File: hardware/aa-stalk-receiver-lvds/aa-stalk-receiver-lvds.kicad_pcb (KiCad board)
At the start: 2 copper layers, 99.1 x 99.1 mm, 63 parts, among them CN1 Conn_01x02, CN2 Conn_01x04, CN3 6P6C, CN4 Conn_01x03, CN5 Conn_01x02, CN6 Conn_01x02, CN7 Conn_01x02, CN8 Conn_01x02, Q1 MMBTA06, Q2 MCH3484, Q3 MCH3484, U1 AZ1117-5.0, U2 MIC5504-3.3YM5, U3 LM4562, U4 FIN1028, U5 MC3486N

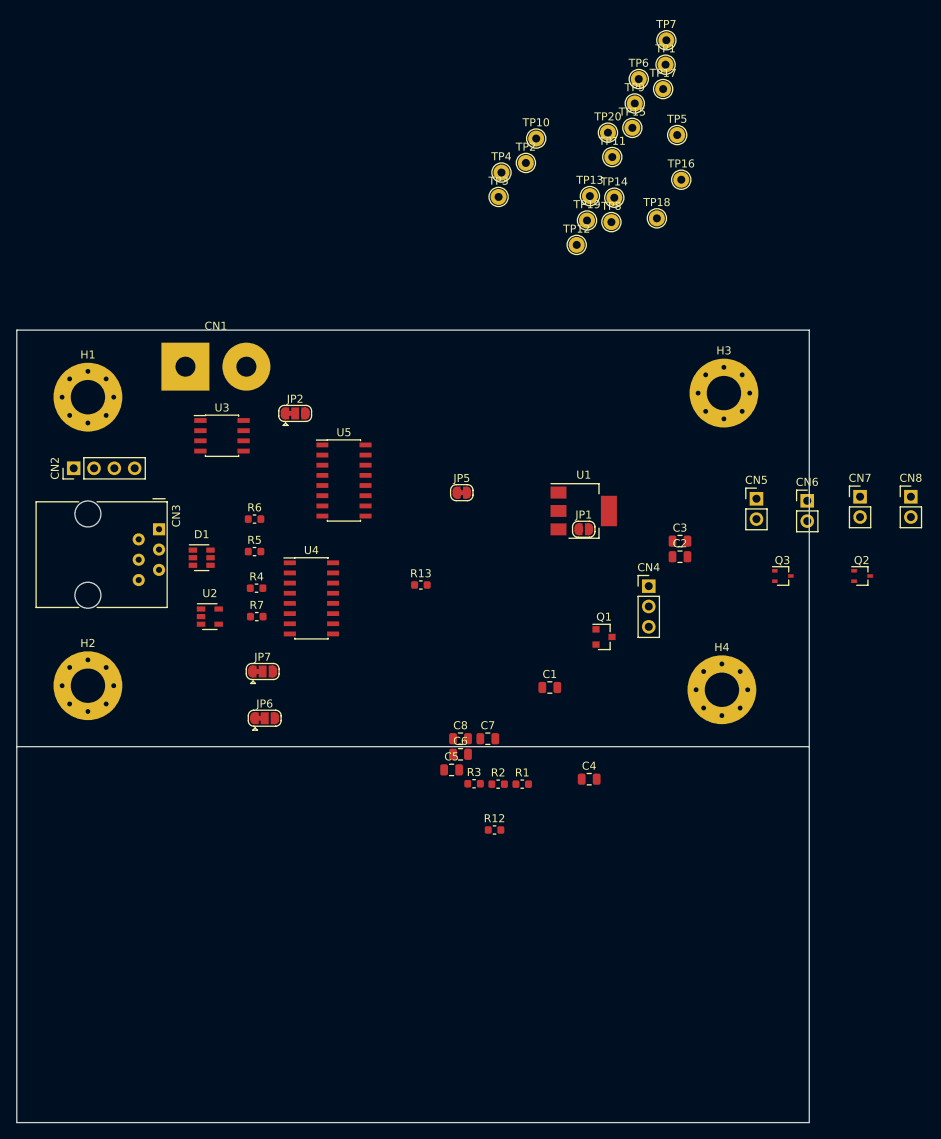
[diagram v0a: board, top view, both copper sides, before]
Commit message: Updates to schematic and layout -- remove test points, add jumpers, iterate layout
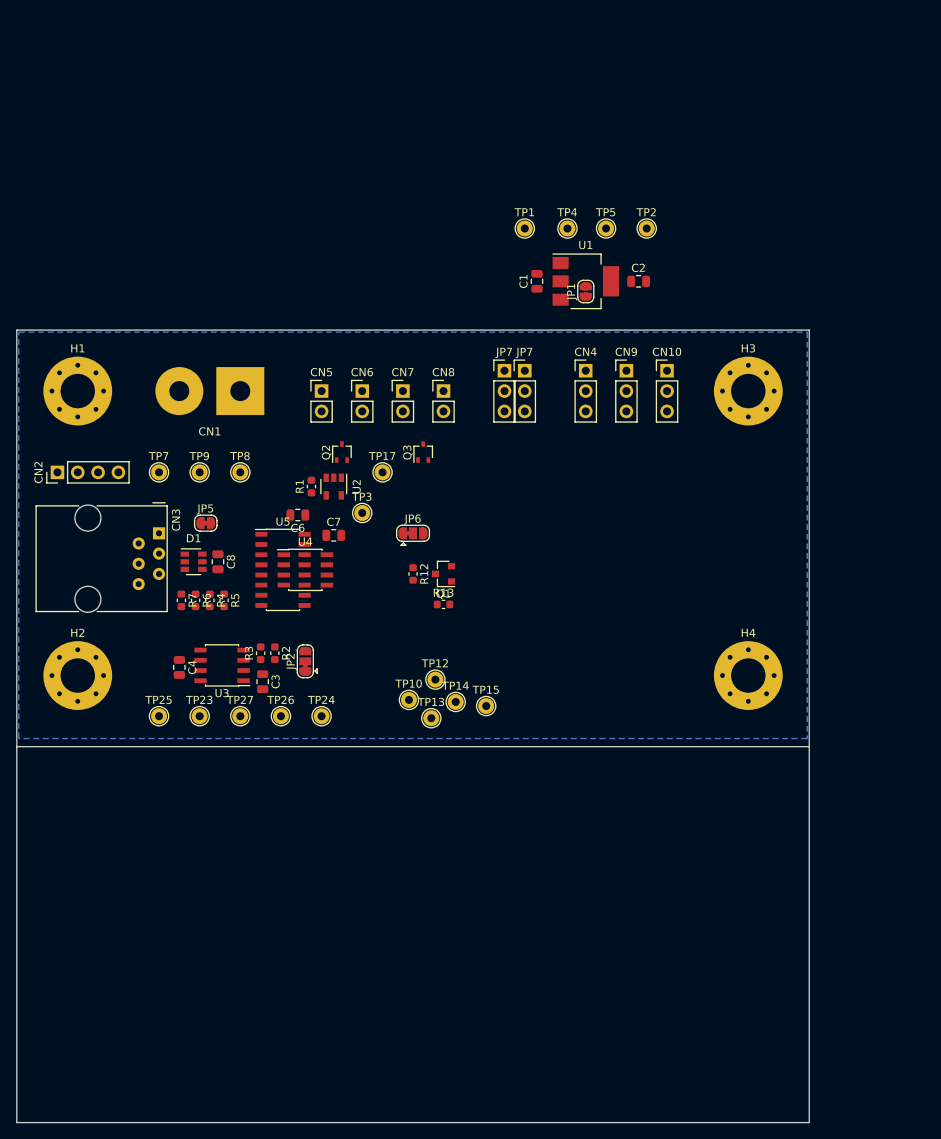
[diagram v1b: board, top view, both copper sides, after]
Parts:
- removed C5: 0.1u, Capacitor_SMD:C_0805_2012Metric
- removed the JP7 at (122.2, 96.0)
- removed TP11, TP16, TP18, TP19, TP20, TP6: TestPoint, TestPoint:TestPoint_THTPad_D2.0mm_Drill1.0mm
- added CN10: Conn_01x03, Connector_PinHeader_2.54mm:PinHeader_1x03_P2.54mm_Vertical, F.Cu at (172.7, 58.4)
- added CN9: Conn_01x03, Connector_PinHeader_2.54mm:PinHeader_1x03_P2.54mm_Vertical, F.Cu at (167.6, 58.4)
- added JP7: Jumper_3_Bridged12, Connector_PinHeader_2.54mm:PinHeader_1x03_P2.54mm_Vertical, F.Cu at (154.9, 58.4)
- added JP7: Jumper_3_Bridged12, Connector_PinHeader_2.54mm:PinHeader_1x03_P2.54mm_Vertical, F.Cu at (152.4, 58.4)
- added TP23: TestPoint, TestPoint:TestPoint_THTPad_D2.0mm_Drill1.0mm, F.Cu at (114.3, 101.6)
- added TP24: TestPoint, TestPoint:TestPoint_THTPad_D2.0mm_Drill1.0mm, F.Cu at (129.5, 101.6)
- added TP25: TestPoint, TestPoint:TestPoint_THTPad_D2.0mm_Drill1.0mm, F.Cu at (109.2, 101.6)
- added TP26: TestPoint, TestPoint:TestPoint_THTPad_D2.0mm_Drill1.0mm, F.Cu at (124.5, 101.6)
- added TP27: TestPoint, TestPoint:TestPoint_THTPad_D2.0mm_Drill1.0mm, F.Cu at (119.4, 101.6)
- C3, C4: value 1u -> 0.1u
- C6: value 0.1u -> 1u
- U4: footprint Package_SO:SOIC-16_3.9x9.9mm_P1.27mm -> Package_SO:SOIC-8_3.9x4.9mm_P1.27mm
- moved TP7 83.3 mm to (109.2, 71.1)
- moved TP15 74.5 mm to (150.1, 100.3)
- moved TP10 72.0 mm to (140.5, 99.6)
- moved TP9 71.3 mm to (114.3, 71.1)
- moved TP13 68.2 mm to (143.3, 101.9)
- moved Q2 66.8 mm to (132.1, 68.6), turned to 90 degrees
- moved TP14 66.1 mm to (146.3, 99.8)
- moved CN8 59.9 mm to (144.8, 61.0)
- moved TP17 59.4 mm to (137.2, 71.1)
- moved CN7 58.7 mm to (139.7, 61.0)
- moved CN6 57.3 mm to (134.6, 61.0)
- moved TP12 57.1 mm to (143.8, 97.0)
- moved CN5 56.0 mm to (129.5, 61.0)
- moved TP8 55.9 mm to (119.4, 71.1)
- moved C3 55.0 mm to (122.2, 97.3), turned to 270 degrees
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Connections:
- C3 pad 1: +5V -> /+2.5A
- C4 pad 1: +3V3 -> /+2.5B
- C6 pad 1: /+2.5B -> +5V
- CN4 pad 1: Net-(CN4-Pad1) -> Net-(CN10-Pad1)
- TP13 pad 1: Net-(CN4-Pad1) -> Net-(CN10-Pad2)
- TP17 pad 1: Net-(CN7-Pad2) -> /PWM_CAP
- TP3 pad 1: /IN_TX_STALK_P -> +3V3
- TP4 pad 1: /IN_TX_STALK_N -> GND
- TP5 pad 1: Net-(CN3-Pad1) -> GND
- TP7 pad 1: /IN_PWM_CAP_N -> Net-(CN3-Pad1)
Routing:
- added copper zone on B.Cu, net GND

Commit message: Latest stalk receiver design -- many tweaks, layout V0 probably done
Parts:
- removed the JP1 at (162.6, 48.5)
- removed the JP7 at (154.9, 58.4)
- removed the JP7 at (152.4, 58.4)
- added C5: 10u, Capacitor_SMD:C_0805_2012Metric, F.Cu at (118.1, 64.8)
- added C9: 10u, Capacitor_SMD:C_0805_2012Metric, F.Cu at (108.0, 64.8)
- added JP1: SolderJumper_2_Open, Jumper:SolderJumper-2_P1.3mm_Open_RoundedPad1.0x1.5mm, F.Cu at (135.9, 69.6)
- added JP1: SolderJumper_2_Open, Jumper:SolderJumper-2_P1.3mm_Open_RoundedPad1.0x1.5mm, F.Cu at (127.0, 71.1)
- added JP1: SolderJumper_2_Open, Jumper:SolderJumper-2_P1.3mm_Open_RoundedPad1.0x1.5mm, F.Cu at (116.8, 71.1)
- added JP1: SolderJumper_2_Open, Jumper:SolderJumper-2_P1.3mm_Open_RoundedPad1.0x1.5mm, F.Cu at (121.9, 71.1)
- added JP7: Jumper_3_Bridged12, Connector_PinHeader_2.54mm:PinHeader_1x03_P2.54mm_Vertical, F.Cu at (144.8, 68.6)
- added JP7: Jumper_3_Bridged12, Connector_PinHeader_2.54mm:PinHeader_1x03_P2.54mm_Vertical, F.Cu at (149.9, 68.6)
- added JP7: Jumper_3_Bridged12, Connector_PinHeader_2.54mm:PinHeader_1x03_P2.54mm_Vertical, F.Cu at (147.3, 68.6)
- Q1: value MMBTA06 -> KST10
- moved TP5 44.4 mm to (154.9, 83.8), turned to 180 degrees
- moved C2 44.1 mm to (132.2, 71.2), turned to 90 degrees
- moved TP4 38.5 mm to (154.9, 78.7), turned to 180 degrees
- moved CN10 38.1 mm to (149.9, 88.9), turned to 270 degrees
- moved TP2 36.4 mm to (154.9, 73.7), turned to 180 degrees
- moved U1 34.1 mm to (136.8, 69.6), turned to 270 degrees
- moved H3 33.0 mm to (149.9, 61.0)
- moved H4 33.0 mm to (149.9, 96.5)
- moved CN9 31.0 mm to (149.9, 83.8), turned to 270 degrees
- moved TP1 27.9 mm to (154.9, 68.6), turned to 180 degrees
- moved C1 25.5 mm to (136.8, 63.5), turned to 0 degrees
- moved CN4 24.0 mm to (149.9, 78.7), turned to 270 degrees
- moved CN6 23.0 mm to (111.8, 58.4)
- moved CN8 23.0 mm to (121.9, 58.4)
- moved CN5 23.0 mm to (106.7, 58.4)
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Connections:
- JP6 pad 1: VDD -> Net-(CN10-Pad1)
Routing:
- net Net-(CN10-Pad1): track 0.00 -> 56.7 mm
- net /IN_TX_STALK_N: track 0.00 -> 44.8 mm, vias 0 -> 1
- net /IN_TX_STALK_P: track 0.00 -> 43.2 mm, vias 0 -> 4
- net Net-(CN4-Pad2): track 0.00 -> 41.6 mm, vias 0 -> 3
- net /PWM_CAP: track 0.00 -> 40.4 mm, vias 0 -> 3
- net /IN_PWM_CAP_P: track 0.00 -> 36.9 mm, vias 0 -> 1
- net /IN_PWM_CAP_N: track 0.00 -> 36.3 mm
- net +5V: track 0.00 -> 34.0 mm, vias 0 -> 6
- net Net-(R2-Pad2): track 0.00 -> 20.3 mm
- net +3V3: track 0.00 -> 19.8 mm
- net /+2.5A: track 0.00 -> 19.1 mm, vias 0 -> 2
- net /+2.5B: track 0.00 -> 18.2 mm
- net GND: track 0.00 -> 18.0 mm, vias 0 -> 19
- net /TX_STALK: track 0.00 -> 16.6 mm, vias 0 -> 2
- net Net-(CN10-Pad2): track 0.00 -> 12.3 mm
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- added copper zone on F.Cu, net +5V
- added copper zone on F.Cu, net VDD
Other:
- board size 99.1 x 99.1 mm -> 67.3 x 50.8 mm
- net class Default: clearance 0.2 -> 0.127; trace_width 0.25 -> 0.381
- net class High current added: clearance 0.127, trace_width 1.016, via_dia 0.8, via_drill 0.4
- rule trace_clearance: 0.2 -> 0.127
- rule trace_min: 0.2 -> 0.127
- rule via_min_size: 0.4 -> 0.6
- board text added: "+2.5V NOM"
- board text added: "+5V"
- board text added: "AMANITA ARCADE STALK RECEIVER V0/2019-05-21"
- board text added: "BRIDGE JP1 TO USE VDD AS +5V"
- board text added: "CN3_VIN"
- board text added: "CN4,9,10: P1: V+ P2: DATA P3: GND"
- board text added: "CN5-8: P1: VDD P2: PWM"
- board text added: "CUT JP5 IF NOT USING CN3_VIN AS +5V"
- board text added: "GND"
- board text added: "JP6 SETS TX_STALK SIGNAL LEVEL 1-2 LED V+ 2-3 +5V"
- board text added: "JP7 DEFAULT BRIDGE 1-2 (UPPER-MIDDLE)"
- board text added: "LED_A DATA"
- board text added: "LED_A SEND"
- board text added: "LED_B RET'N"
- board text added: "LED_C DATA"
- board text added: "LED_C SEND"
- board text added: "NOTE TX_STALK DIFFERENTIAL INPUT IS REVERSED AT RECEIVER!"
- board text added: "ONLY POP ONE OF A) C6, U5 (EIA422) B) R1, C7, U2, U4 (LVDS)"
- board text added: "P1: IN_TX_STALK_P P2: IN_TX_STALK_N P3: IN_PWM_CAP_P P4: IN_PWM_CAP_N"
- board text added: "POP U1, C1, C2 IF NOT USING CN3_VIN OR VDD AS +5V"
- board text added: "PWM_CAP"
- board text added: "R12: TX_STALK PULLUP R13: Q1 I_BASE LIMIT"
- board text added: "R4-R7 OPT 112 OHM TERMINATION R2, R3, C3, C4, U3 IMPROVE CM REJ"
- board text added: "TERM A"
- board text added: "TERM B"
- board text added: "TERM REF"
- board text added: "VDD"
- board text added: "~TX_STALK"

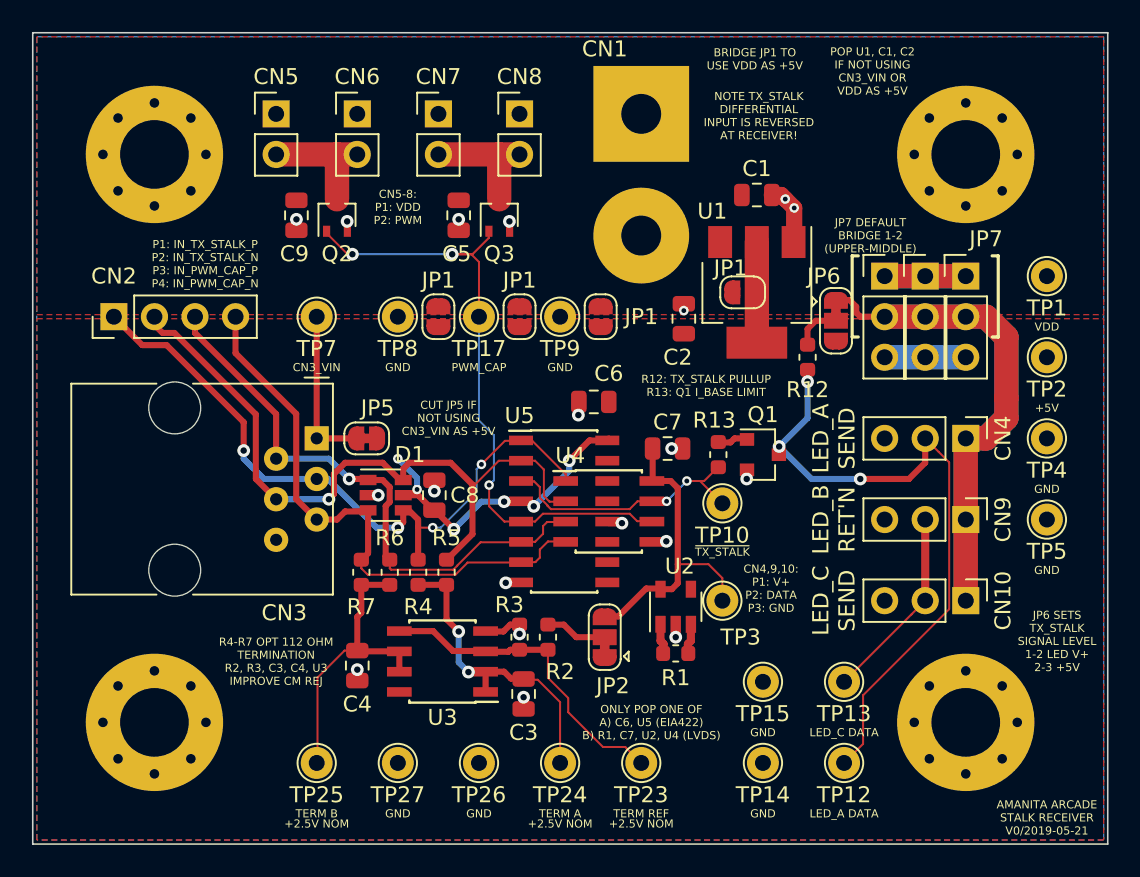
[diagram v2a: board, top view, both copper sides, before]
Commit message: Add power distro board, resolve some todos, finish a coherent layout of the panel receiver
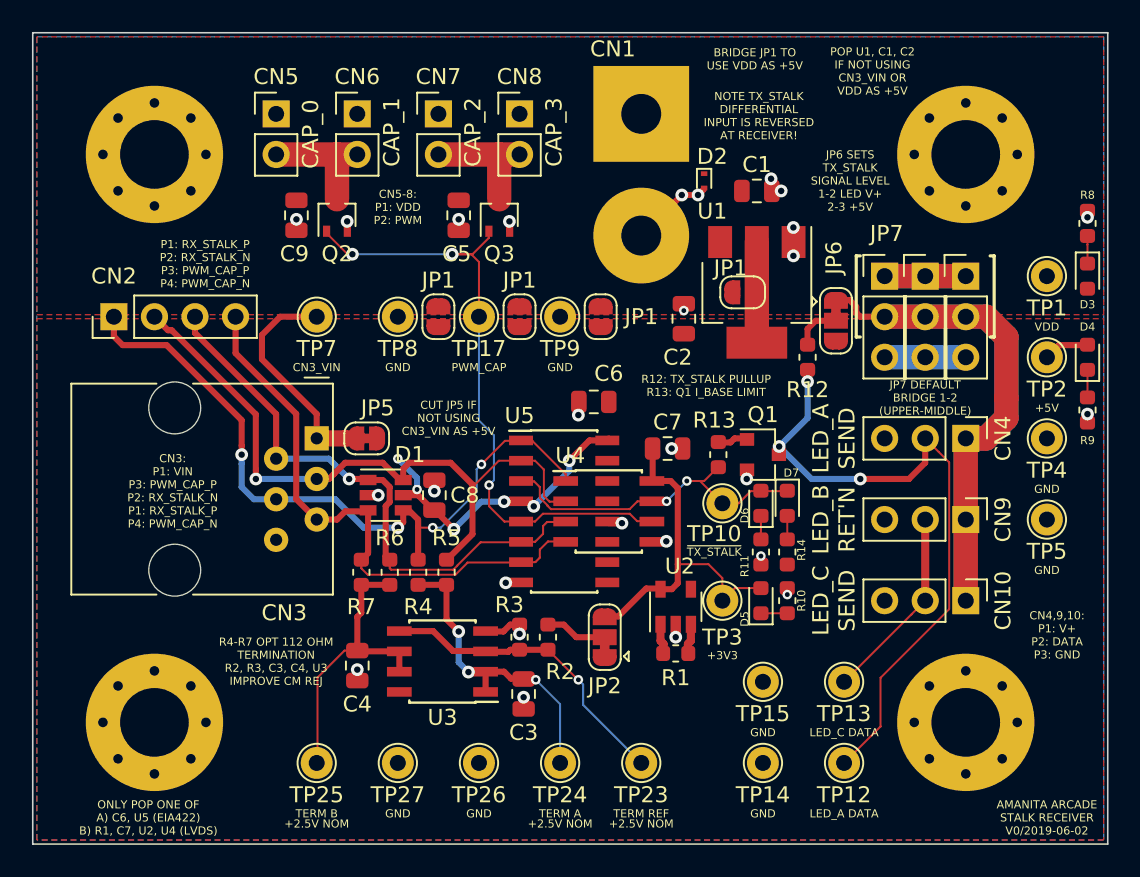
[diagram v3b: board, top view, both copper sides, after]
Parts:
- added D2: D_Zener, aa-stalk-receiver-lvds:D_SOD-923, F.Cu at (133.5, 62.6)
- added D3: LED, Diode_SMD:D_0603_1608Metric, F.Cu at (157.5, 68.6)
- added D4: LED, Diode_SMD:D_0603_1608Metric, F.Cu at (157.5, 73.7)
- added D5: LED, Diode_SMD:D_0603_1608Metric, F.Cu at (137.0, 88.9)
- added D6: LED, Diode_SMD:D_0603_1608Metric, F.Cu at (137.0, 82.8)
- added D7: LED, Diode_SMD:D_0603_1608Metric, F.Cu at (138.7, 82.8)
- added R10: 220, Resistor_SMD:R_0603_1608Metric, F.Cu at (138.7, 88.9)
- added R11: 470, Resistor_SMD:R_0603_1608Metric, F.Cu at (137.0, 85.9)
- added R14: 470, Resistor_SMD:R_0603_1608Metric, F.Cu at (138.7, 85.9)
- added R8: 1.5k, Resistor_SMD:R_0603_1608Metric, F.Cu at (157.5, 65.3)
- added R9: 470, Resistor_SMD:R_0603_1608Metric, F.Cu at (157.5, 77.0)
- moved C1 0.25 mm to (136.8, 63.2)
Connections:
- net /IN_PWM_CAP_N renamed /PWM_CAP_N
- net /IN_PWM_CAP_P renamed /PWM_CAP_P
- net /TX_STALK renamed /RX_STALK
- net Net-(CN10-Pad1) renamed /LED_POWER
- net Net-(CN4-Pad2) renamed /LED_A_DATA
- CN2 pad 1: /IN_TX_STALK_P -> /RX_STALK_P
- CN2 pad 2: /IN_TX_STALK_N -> /RX_STALK_N
- CN3 pad 3: /IN_TX_STALK_P -> /RX_STALK_N
- CN3 pad 4: /IN_TX_STALK_N -> /RX_STALK_P
- D1 pad 4: /IN_TX_STALK_P -> /RX_STALK_P
- D1 pad 6: /IN_TX_STALK_N -> /RX_STALK_N
- R4 pad 1: /IN_TX_STALK_P -> /RX_STALK_P
- R5 pad 1: /IN_TX_STALK_N -> /RX_STALK_N
- U4 pad 1: /IN_TX_STALK_P -> /RX_STALK_P
- U4 pad 2: /IN_TX_STALK_N -> /RX_STALK_N
- U5 pad 1: /IN_TX_STALK_P -> /RX_STALK_P
- U5 pad 2: /IN_TX_STALK_N -> /RX_STALK_N
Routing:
- net /RX_STALK_P: track 0.00 -> 45.0 mm, vias 0 -> 4
- net /IN_TX_STALK_N: track 44.8 -> 0.00 mm, vias 1 -> 0
- net /IN_TX_STALK_P: track 43.2 -> 0.00 mm, vias 4 -> 0
- net /RX_STALK_N: track 0.00 -> 42.7 mm, vias 0 -> 1
- net GND: track 18.0 -> 25.3 mm, vias 19 -> 27
- net /RX_STALK: track 16.6 -> 21.0 mm
- net Net-(CN3-Pad1): track 10.1 -> 14.3 mm
- net +5V: track 34.0 -> 36.9 mm
- net +3V3: track 19.8 -> 22.5 mm
- net Net-(D5-Pad1): track 0.00 -> 1.92 mm
- net Net-(D4-Pad1): track 0.00 -> 1.75 mm
- net Net-(D3-Pad1): track 0.00 -> 1.75 mm
- net Net-(D7-Pad2): track 0.00 -> 1.50 mm
- net Net-(D6-Pad1): track 0.00 -> 1.50 mm
- net Net-(R2-Pad2): track 20.3 -> 19.5 mm, vias 0 -> 1
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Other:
- board text added: "+3V3"
- board text added: "AMANITA ARCADE STALK RECEIVER V0/2019-06-02"
- board text added: "CAP_0"
- board text added: "CAP_1"
- board text added: "CAP_2"
- board text added: "CAP_3"
- board text added: "CN3: P1: VIN P3: PWM_CAP_P P2: RX_STALK_N P1: RX_STALK_P P4: PWM_CAP_N"
- board text added: "P1: RX_STALK_P P2: RX_STALK_N P3: PWM_CAP_P P4: PWM_CAP_N"
- board text removed: "AMANITA ARCADE STALK RECEIVER V0/2019-05-21"
- board text removed: "P1: IN_TX_STALK_P P2: IN_TX_STALK_N P3: IN_PWM_CAP_P P4: IN_PWM_CAP_N"

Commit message: Update to use a shared schematic component/footprint library
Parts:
- CN3: footprint aa-stalk-receiver-lvds:6P6C_Assmann_A-2014-1-4 -> aa-shared:6P6C_Assmann_A-2014-1-4
- D2: footprint aa-stalk-receiver-lvds:D_SOD-923 -> aa-shared:D_SOD-923
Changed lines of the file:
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@@
     )
   )
-  (module aa-stalk-receiver-lvds:D_SOD-923 (layer F.Cu)
+  (module aa-shared:D_SOD-923 (layer F.Cu)
     (at 133.477 62.611 270)
     (descr SOD-323)
@@
       (net 20 "Net-(CN10-Pad2)"))
   )
-  (module aa-stalk-receiver-lvds:6P6C_Assmann_A-2014-1-4 (layer F.Cu)
+  (module aa-shared:6P6C_Assmann_A-2014-1-4 (layer F.Cu)
     (at 109.22 78.74 270)
     (descr http://www.assmann-wsw.com/fileadmin/datasheets/ASS_7327_CO.pdf)
